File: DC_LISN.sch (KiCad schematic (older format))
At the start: 50 parts, among them M1 MountingHole, M2 MountingHole, M3 MountingHole, M4 MountingHole, X1 PCB.SMAFRA.HT, X2 B8B-EH-A, X3 B8B-EH-A, X4 575-4, X5 575-4, X6 575-4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

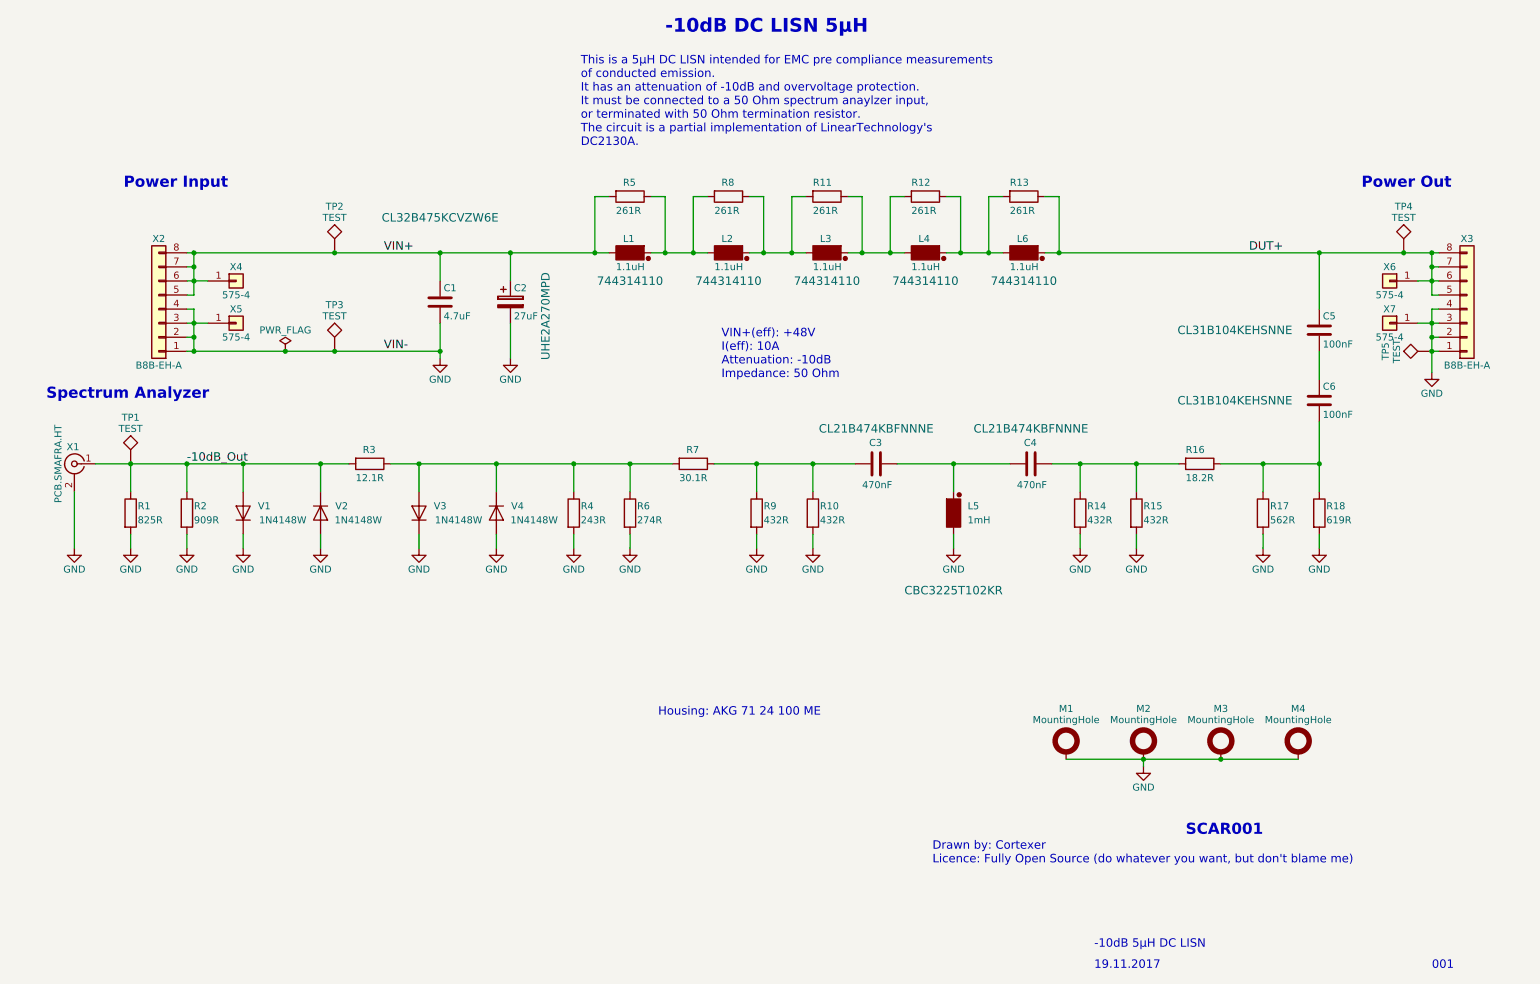
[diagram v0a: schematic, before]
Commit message: Licensing: Changed to OSHW Changed licensing to open source hardware. Added an additional signal input for use as standalone attenuator.
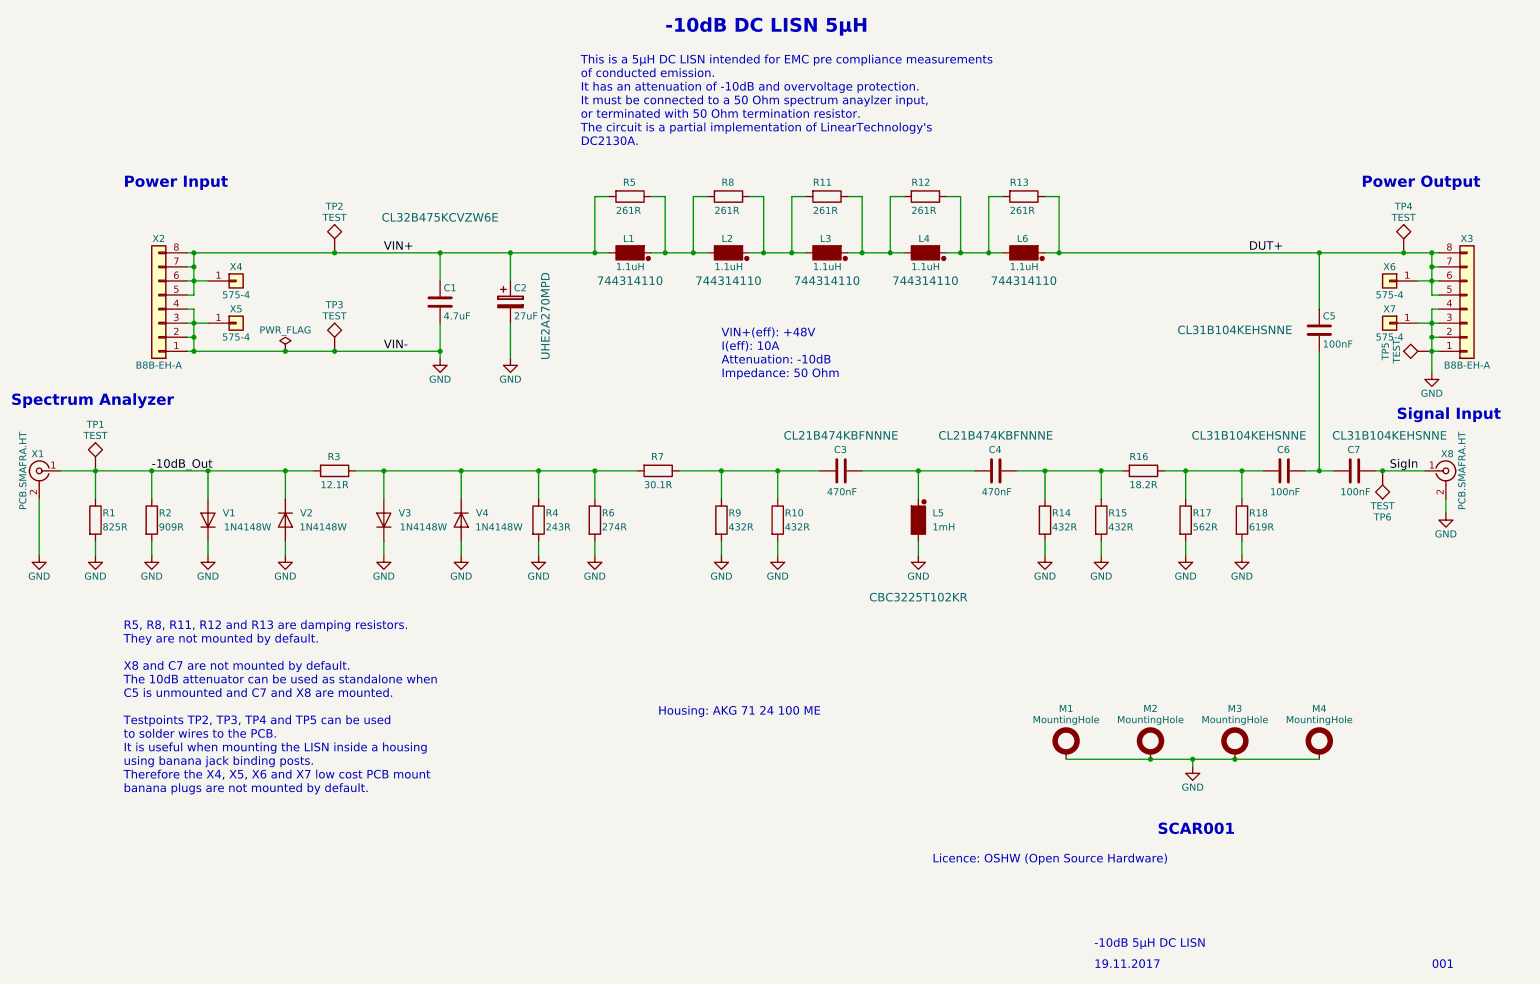
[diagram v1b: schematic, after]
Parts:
- added C7: 100nF, MST_Lib:C_1206, symbol C
- added TP6: TEST, MST_Lib:TP_1mm, symbol TEST
- added X8: PCB.SMAFRA.HT, MST_Lib:X_SMA_THT_Jack_Straight_PCB.SMAFRA.HT, symbol Conn_Coaxial
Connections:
- net GND: now also X8.2 (Ext)
- net at C5.2, C6.1: now also C7.2
- new net SigIn: C7.1, TP6.1, X8.1 (In)
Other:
- note added: "Licence: OSHW (Open Source Hardware)"
- note added: "Power Output"
- note added: "R5, R8, R11, R12 and R13 are damping resistors.\nThey are not mounted by default.\n\nX8 and C7 are not mounted by default.\nThe 10dB attenuator can be used as standalone when\nC5 is unmounted and C7 and X8 are mounted.\n\nTestpoints TP2, TP3, TP4 and TP5 can be used\nto solder wires to the PCB.\nIt is useful when mounting the LISN inside a housing\nusing banana jack binding posts.\nTherefore the 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"
- note added: "Signal Input"
- note removed: "Drawn by: Cortexer\nLicence: Fully Open Source (do whatever you want, but don't blame me)"
- note removed: "Power Out"
- moved on the sheet: C3, C4, C6, L5, M2, M3, M4, R1, R10, R14, R15, R16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

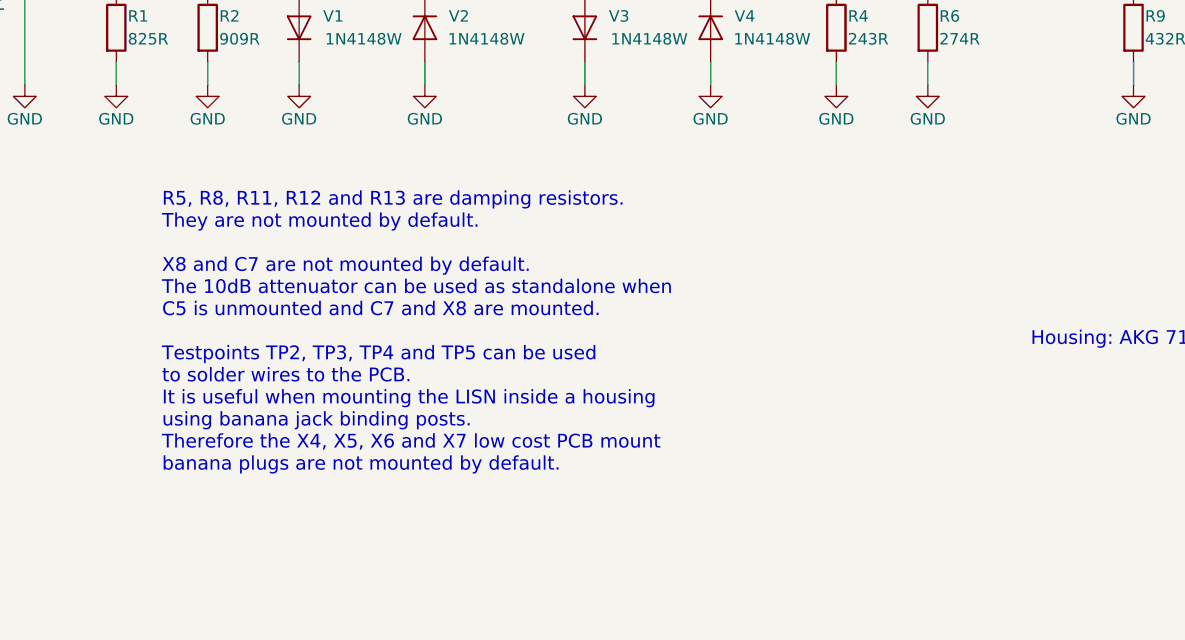
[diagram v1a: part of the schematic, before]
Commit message: Schematic: Added comments
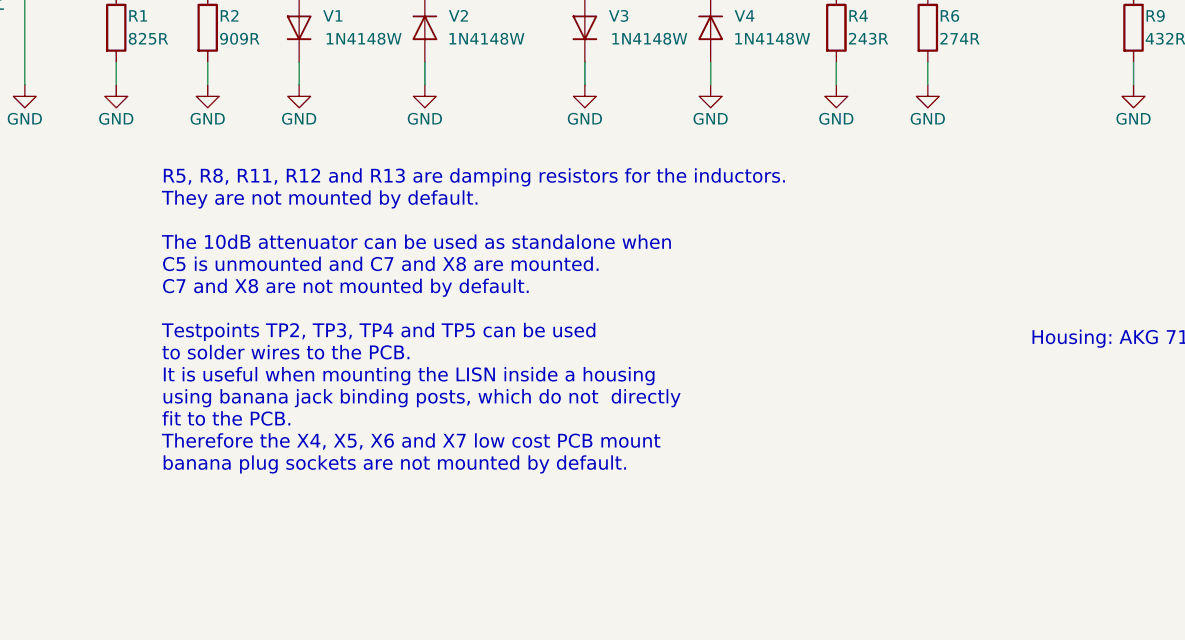
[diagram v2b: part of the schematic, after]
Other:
- note added: "R5, R8, R11, R12 and R13 are damping resistors for the inductors.\nThey are not mounted by default.\n\nThe 10dB attenuator can be used as standalone when\nC5 is unmounted and C7 and X8 are mounted.\nC7 and X8 are not mounted by default.\n\nTestpoints TP2, TP3, TP4 and TP5 can be used\nto solder wires to the PCB.\nIt is useful when mounting the LISN inside a housing\nusing banana jack binding post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"
- note removed: "R5, R8, R11, R12 and R13 are damping resistors.\nThey are not mounted by default.\n\nX8 and C7 are not mounted by default.\nThe 10dB attenuator can be used as standalone when\nC5 is unmounted and C7 and X8 are mounted.\n\nTestpoints TP2, TP3, TP4 and TP5 can be used\nto solder wires to the PCB.\nIt is useful when mounting the LISN inside a housing\nusing banana jack binding posts.\nTherefore the 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"
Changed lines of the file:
@@
 Data
 89 50 4E 47 0D 0A 1A 0A 00 00 00 0D 49 48 44 52 00 00 00 BE 00 00 00 C8 08 03 00 00 00 61 D1 AB
-73 00 00 00 03 73 42 49 54 08 08 08 DB E1 4F E0 00 00 00 1B 50 4C 54 45 02 00 00 00 99 B0 00 99
-B1 00 9A B1 00 98 AF 00 9A B0 00 98 B0 00 99 AF 00 9A AF AE 59 D3 29 00 00 00 01 74 52 4E 53 00
+73 00 00 00 03 73 42 49 54 08 08 08 DB E1 4F E0 00 00 00 1B 50 4C 54 45 01 00 00 00 99 B0 00 99
+B1 00 9A B1 00 98 AF 00 9A B0 00 98 B0 00 99 AF 00 9A AF 1D CD FE EA 00 00 00 01 74 52 4E 53 00
 40 E6 D8 66 00 00 00 09 70 48 59 73 00 00 0F 3C 00 00 0F 3C 01 17 3A 9F 59 00 00 06 24 49 44 41
 54 78 9C ED 9D EB BA A3 2A 0C 86 05 07 F5 FE AF 78 EF 56 D1 90 04 09 4A A0 3C 8B FC 98 45 21 7C
@@
 Connection ~ 9800 4100
 Text Notes 1300 6400 0    60   ~ 0
-R5, R8, R11, R12 and R13 are damping resistors.\nThey are not mounted by default.\n\nX8 and C7 are not mounted by default.\nThe 10dB attenuator can be used as standalone when\nC5 is unmounted and C7 and X8 are mounted.\n\nTestpoints TP2, TP3, TP4 and TP5 can be used\nto solder wires to the PCB.\nIt is useful when mounting the LISN inside a housing\nusing banana jack binding posts.\nTherefore the X4, X5, X6 and X7 low cost PCB mount\nbanana plugs are not mounted by default.
+R5, R8, R11, R12 and R13 are damping resistors for the inductors.\nThey are not mounted by default.\n\nThe 10dB attenuator can be used as standalone when\nC5 is unmounted and C7 and X8 are mounted.\nC7 and X8 are not mounted by default.\n\nTestpoints TP2, TP3, TP4 and TP5 can be used\nto solder wires to the PCB.\nIt is useful when mounting the LISN inside a housing\nusing banana jack binding posts, which do not  directly\nfit to the PCB.\nTherefore the X4, X5, X6 and X7 low cost PCB mount\nbanana plug sockets are not mounted by default.
 $Comp
 L TEST TP6

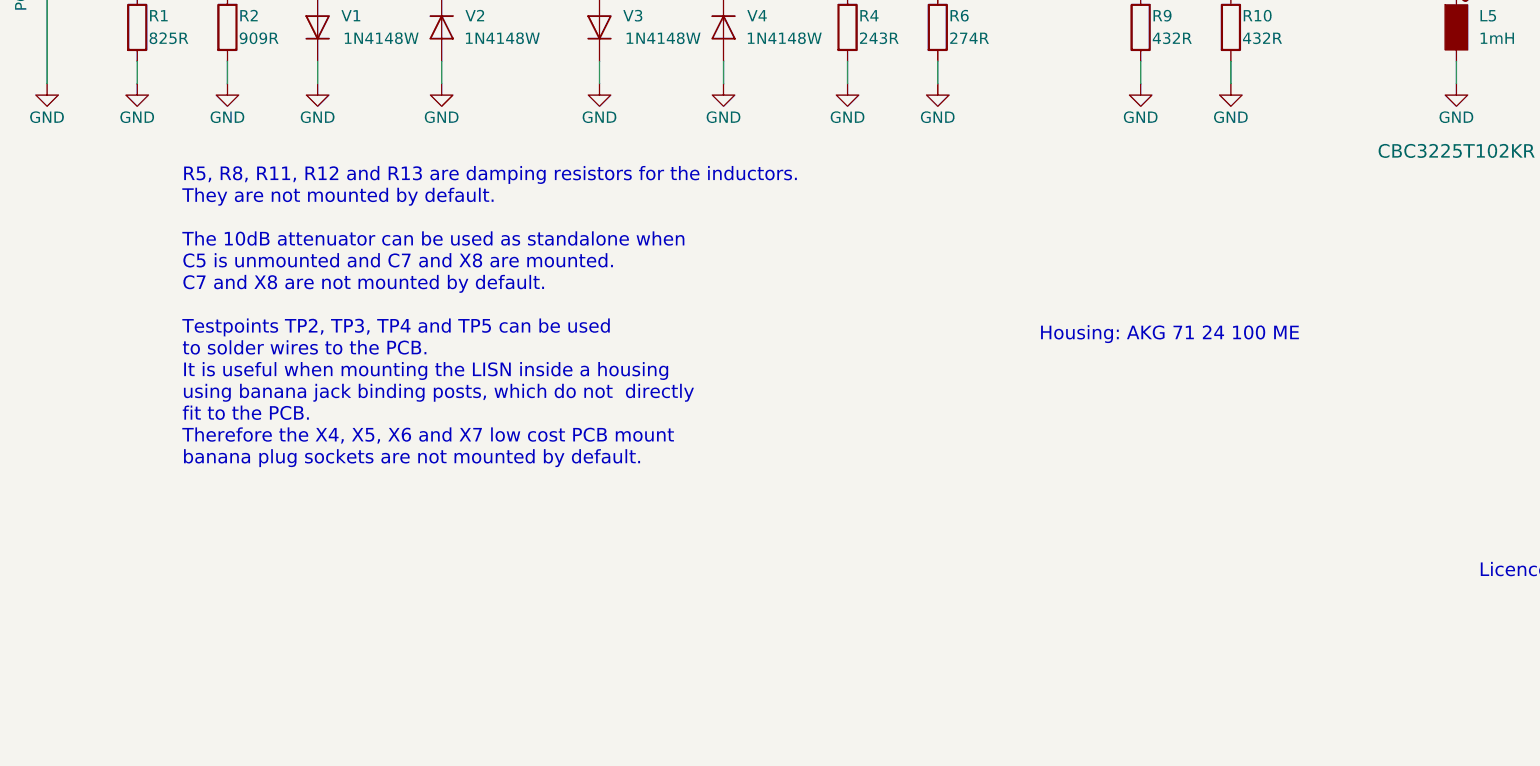
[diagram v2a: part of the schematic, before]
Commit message: Schematic: Improved comments
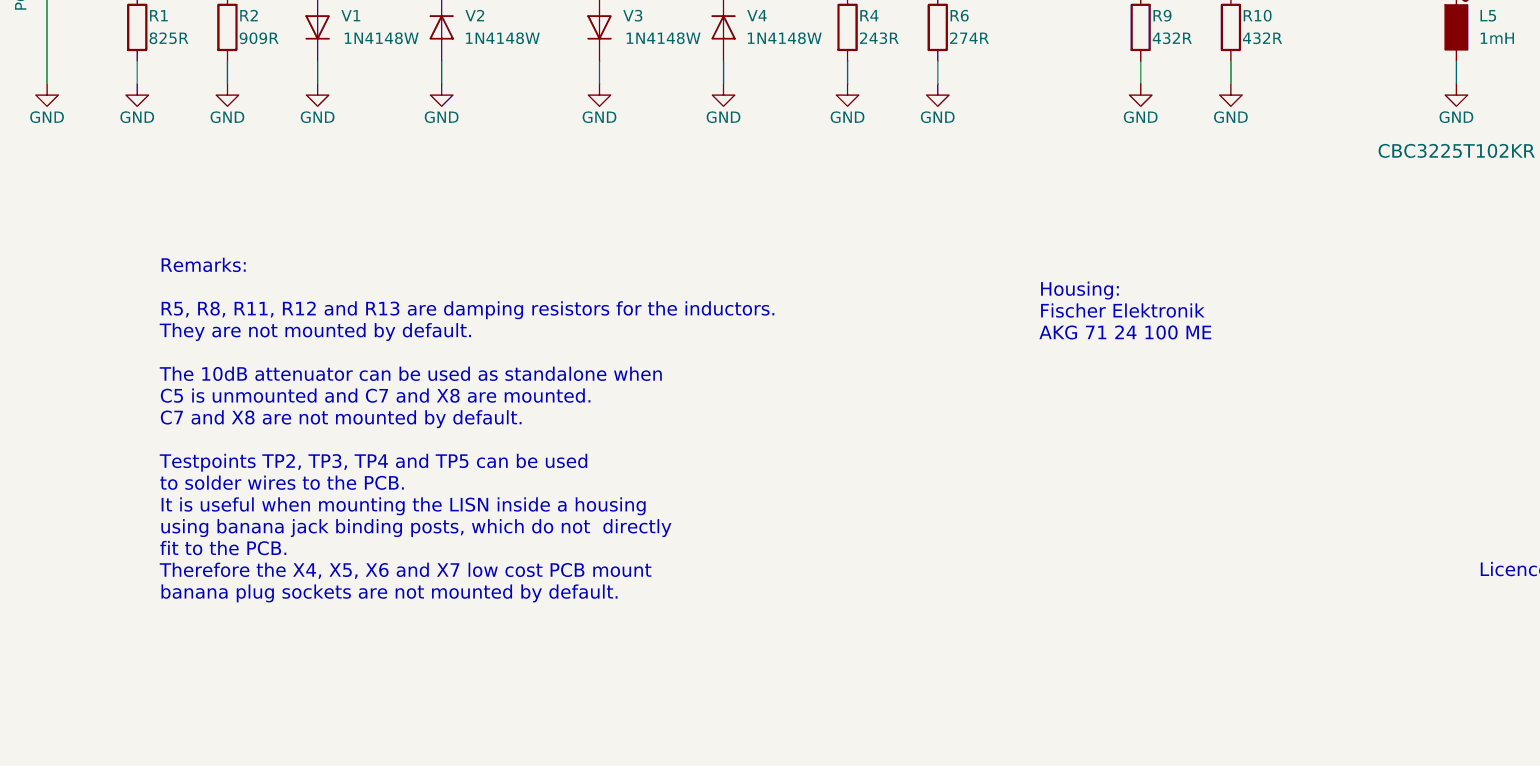
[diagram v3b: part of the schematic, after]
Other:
- note added: "Housing:\nFischer Elektronik\nAKG 71 24 100 ME"
- note added: "Remarks:\n\nR5, R8, R11, R12 and R13 are damping resistors for the inductors.\nThey are not mounted by default.\n\nThe 10dB attenuator can be used as standalone when\nC5 is unmounted and C7 and X8 are mounted.\nC7 and X8 are not mounted by default.\n\nTestpoints TP2, TP3, TP4 and TP5 can be used\nto solder wires to the PCB.\nIt is useful when mounting the LISN inside a housing\nusing banana jack 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"
- note removed: "Housing: AKG 71 24 100 ME"
- note removed: "R5, R8, R11, R12 and R13 are damping resistors for the inductors.\nThey are not mounted by default.\n\nThe 10dB attenuator can be used as standalone when\nC5 is unmounted and C7 and X8 are mounted.\nC7 and X8 are not mounted by default.\n\nTestpoints TP2, TP3, TP4 and TP5 can be used\nto solder wires to the PCB.\nIt is useful when mounting the LISN inside a housing\nusing banana jack binding post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"
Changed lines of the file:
@@
 Connection ~ 2450 4100
 Text Notes 5100 5850 0    60   ~ 0
-Housing: AKG 71 24 100 ME
+Housing:\nFischer Elektronik\nAKG 71 24 100 ME
 Text Notes 8650 6700 0    79   ~ 16
 SCAR001
@@
 Data
 89 50 4E 47 0D 0A 1A 0A 00 00 00 0D 49 48 44 52 00 00 00 BE 00 00 00 C8 08 03 00 00 00 61 D1 AB
-73 00 00 00 03 73 42 49 54 08 08 08 DB E1 4F E0 00 00 00 1B 50 4C 54 45 01 00 00 00 99 B0 00 99
-B1 00 9A B1 00 98 AF 00 9A B0 00 98 B0 00 99 AF 00 9A AF 1D CD FE EA 00 00 00 01 74 52 4E 53 00
+73 00 00 00 03 73 42 49 54 08 08 08 DB E1 4F E0 00 00 00 1B 50 4C 54 45 02 00 00 00 99 B0 00 99
+B1 00 9A B1 00 98 AF 00 9A B0 00 98 B0 00 99 AF 00 9A AF AE 59 D3 29 00 00 00 01 74 52 4E 53 00
 40 E6 D8 66 00 00 00 09 70 48 59 73 00 00 0F 3C 00 00 0F 3C 01 17 3A 9F 59 00 00 06 24 49 44 41
 54 78 9C ED 9D EB BA A3 2A 0C 86 05 07 F5 FE AF 78 EF 56 D1 90 04 09 4A A0 3C 8B FC 98 45 21 7C
@@
 	9700 4100 9900 4100
 Connection ~ 9800 4100
-Text Notes 1300 6400 0    60   ~ 0
-R5, R8, R11, R12 and R13 are damping resistors for the inductors.\nThey are not mounted by default.\n\nThe 10dB attenuator can be used as standalone when\nC5 is unmounted and C7 and X8 are mounted.\nC7 and X8 are not mounted by default.\n\nTestpoints TP2, TP3, TP4 and TP5 can be used\nto solder wires to the PCB.\nIt is useful when mounting the LISN inside a housing\nusing banana jack binding posts, which do not  directly\nfit to the PCB.\nTherefore the X4, X5, X6 and X7 low cost PCB mount\nbanana plug sockets are not mounted by default.
+Text Notes 1200 7000 0    60   ~ 0
+Remarks:\n\nR5, R8, R11, R12 and R13 are damping resistors for the inductors.\nThey are not mounted by default.\n\nThe 10dB attenuator can be used as standalone when\nC5 is unmounted and C7 and X8 are mounted.\nC7 and X8 are not mounted by default.\n\nTestpoints TP2, TP3, TP4 and TP5 can be used\nto solder wires to the PCB.\nIt is useful when mounting the LISN inside a housing\nusing banana jack binding posts, which do not  directly\nfit to the PCB.\nTherefore the X4, X5, X6 and X7 low cost PCB mount\nbanana plug sockets are not mounted by default.
 $Comp
 L TEST TP6
